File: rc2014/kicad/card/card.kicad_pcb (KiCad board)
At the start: 4 copper layers, 63.5 x 102.6 mm, 21 parts, among them J1 Conn_RC40_Male, J2 VideoMezzanine14, SW1 SW_DIP_x07, U1 74HCT688, U2 SN74LVC8T245PWR, U3 SN74LVC8T245PWR, U4 VDC-II-card

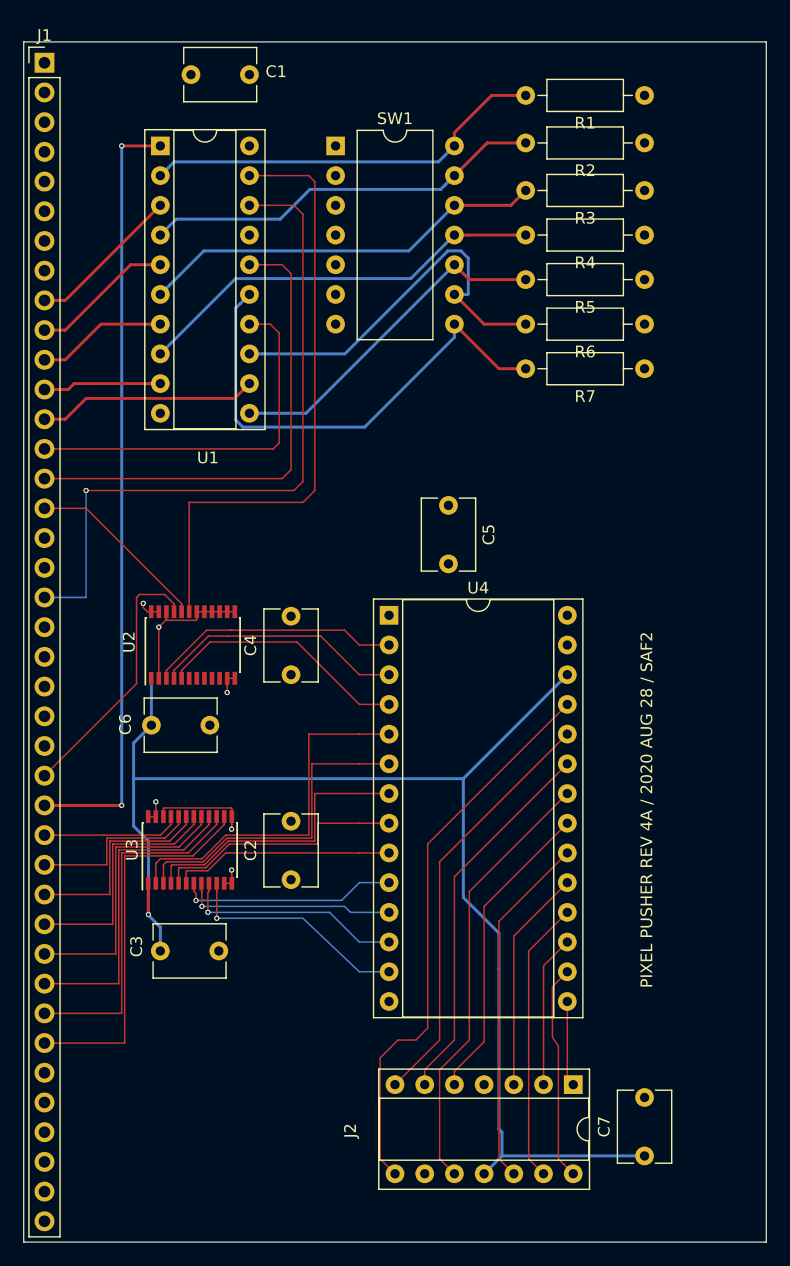
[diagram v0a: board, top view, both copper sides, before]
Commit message: Rev 4B of PCB layout.
- Fix missing pin 1 indicators.
- Fix missing 3.3V supply connection on U2.
- Fix DIP switch footprint size.
- Rename PCB to BX-PLORER
  - Pixel Pusher will be (BX-PLORER + VGA mezzanine).
  - Separate mezzanine planned for PS/2 keyboard and mouse.
- Convert J2 from 14-pin DIP to 14-pin female header.  (Same pinout
  though.)
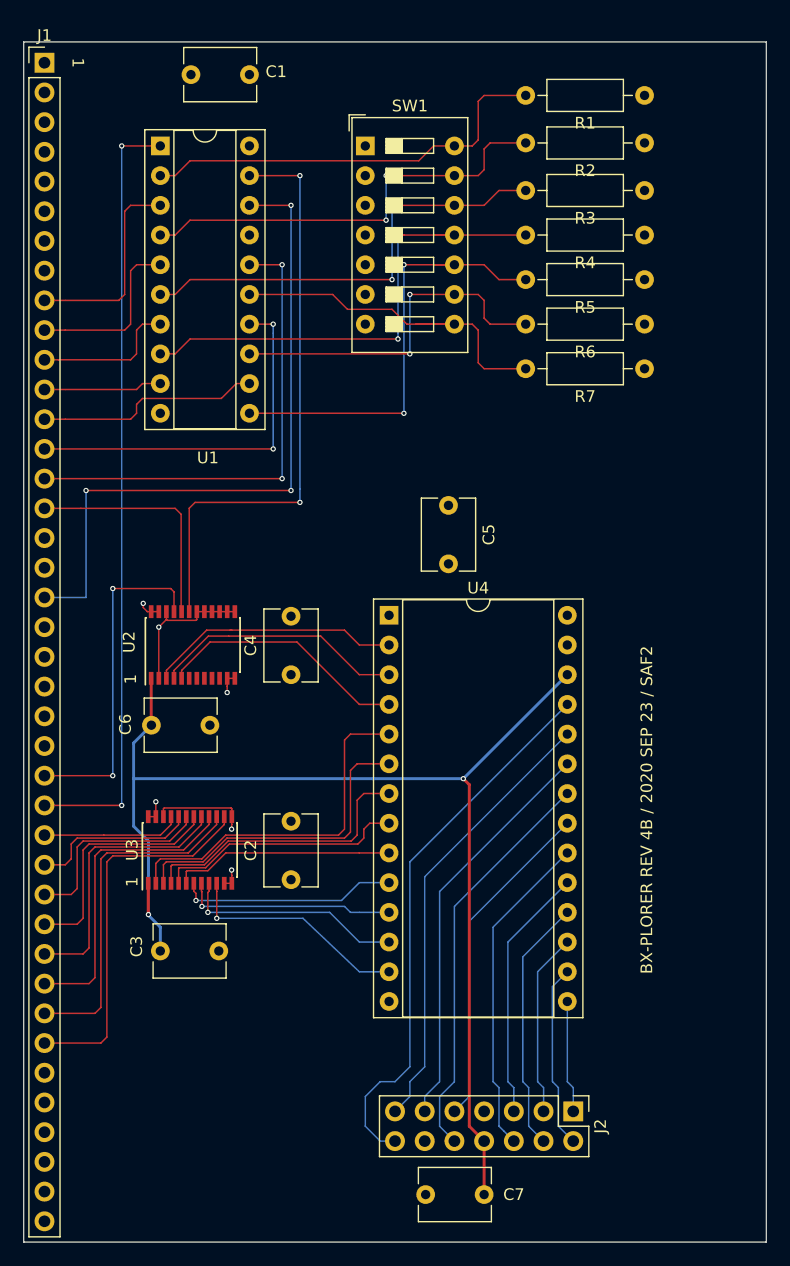
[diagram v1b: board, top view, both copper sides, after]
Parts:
- J2: footprint Package_DIP:DIP-14_W7.62mm_Socket -> Connector_PinHeader_2.54mm:PinHeader_2x07_P2.54mm_Vertical
- SW1: footprint Package_DIP:DIP-14_W10.16mm -> Button_Switch_THT:SW_DIP_SPSTx07_Slide_9.78x19.96mm_W7.62mm_P2.54mm
- moved C7 14.1 mm to (64.8, 124.0), turned to 180 degrees
- moved SW1 2.54 mm to (54.6, 34.3)
- moved J2 2.29 mm to (72.4, 116.8)
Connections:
- J2 pad 11: +3V3 -> /B0
- J2 pad 12: /G0 -> Net-(J2-Pad12)
- J2 pad 13: /G2 -> /HSYNC
- J2 pad 14: /R1 -> /VSYNC
- J2 pad 2: /R0 -> /R1
- J2 pad 3: /G1 -> /R0
- J2 pad 4: GNDD -> /G2
- J2 pad 5: /B2 -> /G1
- J2 pad 6: /B0 -> /G0
- J2 pad 7: /HSYNC -> GNDD
- J2 pad 8: /VSYNC -> +3V3
- J2 pad 9: Net-(J2-Pad9) -> /B2
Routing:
- net +3V3: track 116.4 -> 104.7 mm, vias 1 -> 2
- net Net-(R7-Pad2): track 42.2 -> 31.2 mm
- net Net-(R5-Pad2): track 29.4 -> 38.6 mm, vias 0 -> 2
- net Net-(R4-Pad2): track 35.5 -> 42.7 mm, vias 0 -> 2
- net Net-(J1-Pad25): track 22.8 -> 28.9 mm, vias 0 -> 2
- net Net-(J1-Pad16): track 15.8 -> 20.3 mm
- net Net-(J1-Pad9): track 13.3 -> 17.4 mm
- net Net-(R3-Pad2): track 34.9 -> 38.6 mm, vias 0 -> 2
- net Net-(R6-Pad2): track 34.0 -> 30.6 mm, vias 0 -> 2
- net Net-(R2-Pad2): track 34.5 -> 37.8 mm, vias 0 -> 2
- net /B1: track 37.6 -> 34.8 mm
- net /R1: track 18.5 -> 15.7 mm
- net /R0: track 13.0 -> 15.7 mm
- net /G1: track 19.2 -> 21.9 mm
- net Net-(J1-Pad10): track 12.2 -> 14.9 mm
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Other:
- board text added: "1"
- board text added: "BX-PLORER REV 4B / 2020 SEP 23 / SAF2"
- board text removed: "PIXEL PUSHER REV 4A / 2020 AUG 28 / SAF2"
